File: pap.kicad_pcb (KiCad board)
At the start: 2 copper layers, 60 x 60 mm, 70 parts, among them J51 Conn_01x04, J52 Conn_01x02, J53 Conn_01x02, J54 RJ45, J55 RJ45, J56 RJ12, U1 powerstep01

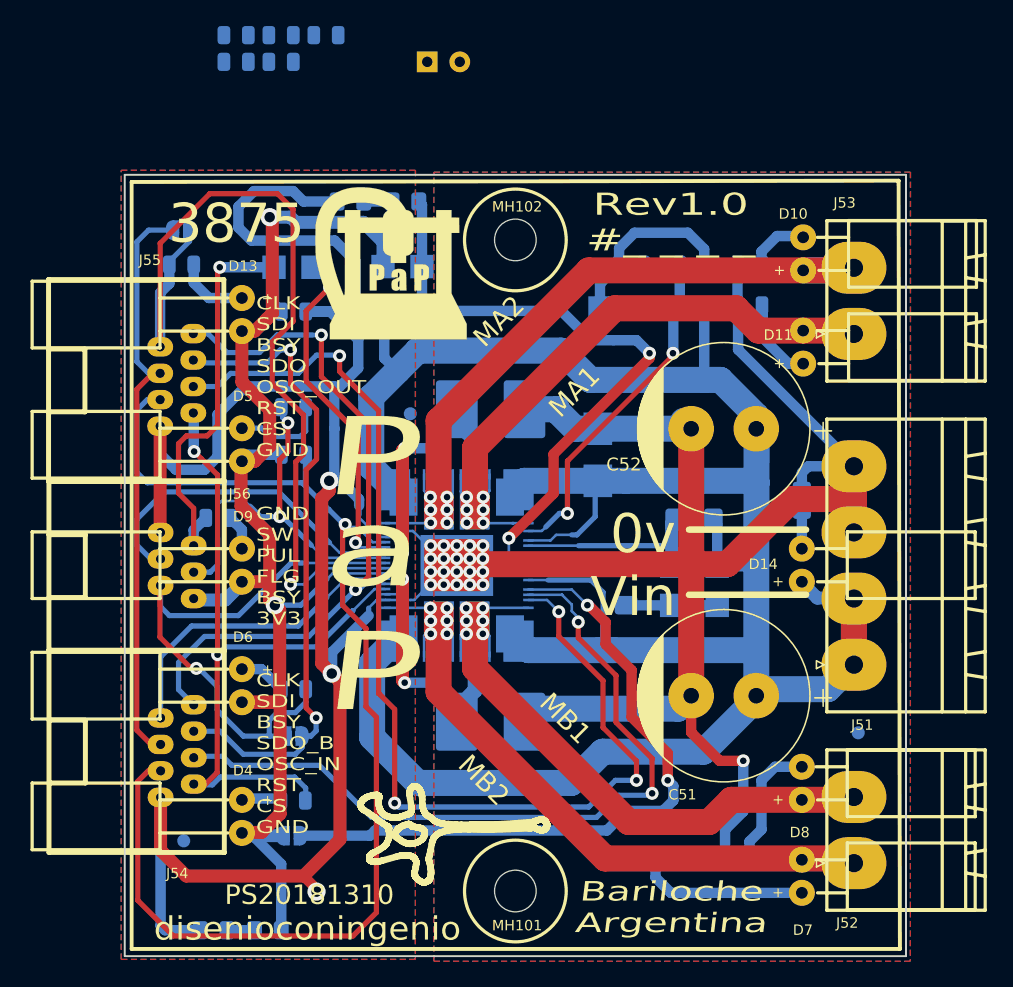
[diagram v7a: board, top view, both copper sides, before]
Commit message: termino ruteo, genero gerbers y drills, y entrego
Listo pisto, lo dejo asi, ya lo revise varias veces, agregue los
desacoples y el bulk pendiente, coloreo leds con nuevo 3d, genero
gerners, y agrego valores a los componentes. ha y tambien dejo PTH los
agujeros de los tornillos, quedan mejor. y no mucho mas.. entrego ya!
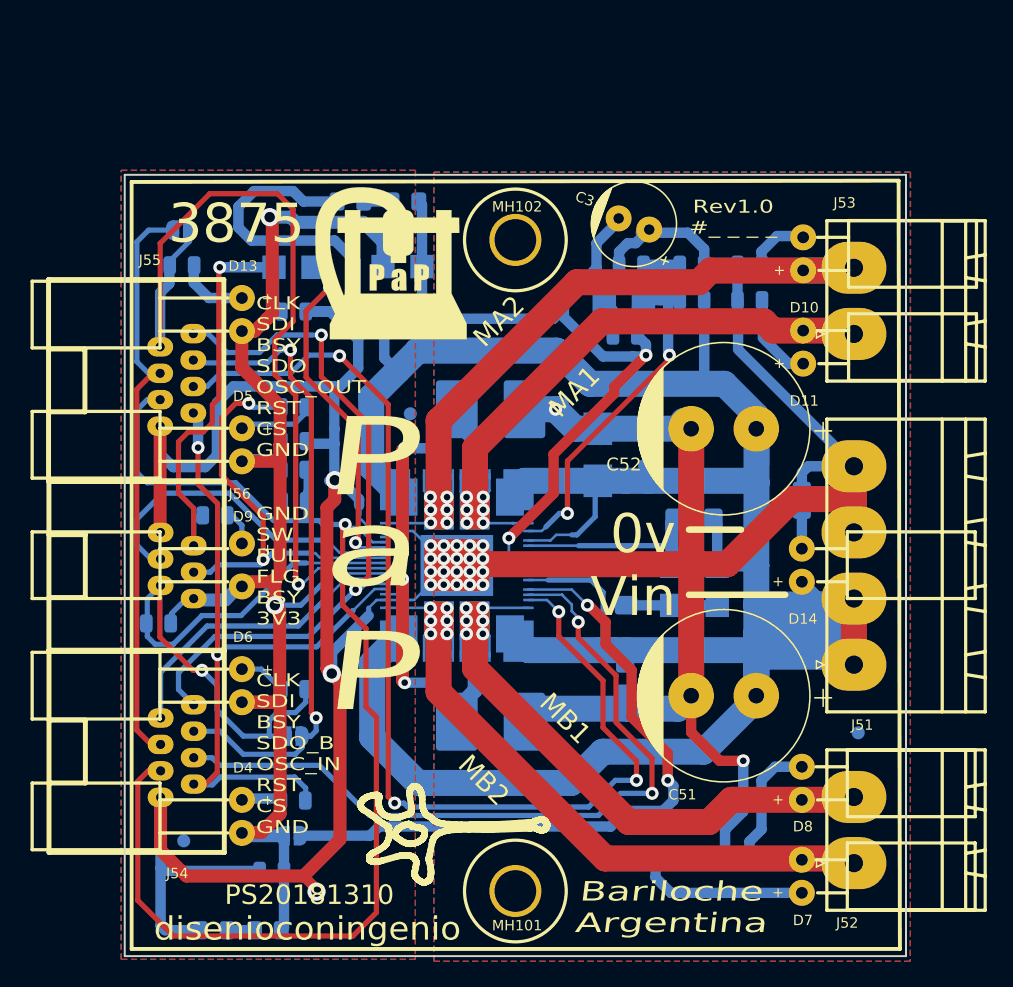
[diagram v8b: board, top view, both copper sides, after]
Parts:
- removed R204: R, pap:R_0805_2012Metric
- added C10: C, pap:C_0805_2012Metric, B.Cu at (130.9, 121.2)
- added C11: C, pap:C_0805_2012Metric, B.Cu at (132.6, 103.9)
- added R17: 100e, pap:R_0805_2012Metric, B.Cu at (96.9, 89.4)
- C1: value C -> 10n
- C3: footprint Capacitor_THT:CP_Radial_D6.3mm_P2.50mm -> pap:CP_Radial_D6.3mm_P2.50mm; moved to F.Cu
- C4, C5: value C -> 220n
- C6, C9: value C -> 100n
- D10, D7: footprint pap:led5p_enchufable -> pap:led5x2_enchufable_amarillo
- D11, D8: footprint pap:led5p_enchufable -> pap:led5x2_enchufable_verde
- D12: value D_Zener -> 3v3
- D13, D4: footprint pap:led5p_rj -> pap:led5x2_rj_verde
- D14: footprint pap:led5p_enchufable -> pap:led5x2_enchufable_rojo
- D5, D6: footprint pap:led5p_rj -> pap:led5x2_rj_amarillo
- D9: footprint pap:led5p_rj -> pap:led5x2_rj_rojo_abierto
- MH101, MH102: value MountingHole -> 3mm
- R1, R11, R12, R13, R14: value R -> 10k
- R10, R5, R8, R9: value R -> 100e
- R16: renamed from R203; value R -> 100e
- R18: renamed from R202; value R -> 10k
- R2: value R -> 1k5
- R3, R4: value R -> 0.1e
- R6: value R -> 100k
- R7: value R -> 3k3
- moved C2 64.3 mm to (103.8, 135.9)
- moved R15 43.5 mm to (95.1, 116.9)
- moved C9 36.0 mm to (105.5, 107.5), turned to 180 degrees
- moved C7 35.1 mm to (130.9, 94.8)
- moved C8 29.1 mm to (105.5, 102.9), turned to 180 degrees
- moved C3 21.4 mm to (132.8, 86.7), turned to 160 degrees
- moved R1 1.15 mm to (105.5, 105.1)
- moved D12 0.58 mm to (130.8, 92.2)
- moved R14 0.40 mm to (140.5, 92.1)
- moved R6 0.40 mm to (136.1, 92.1)
- moved R16 0.31 mm to (99.4, 108.6)
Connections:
- C3 pad 1: G3V3 -> G85V
- C3 pad 2: 3V3 -> 15v
- C8 pad 1: G85V -> G3V3
- C8 pad 2: 15v -> 3V3
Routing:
- net 85v: track 202.1 -> 222.1 mm
- net 15v: track 52.8 -> 63.2 mm
- net G3V3: track 153.2 -> 163.3 mm
- net 3V3: track 104.7 -> 113.4 mm
- net /connector/Busy: track 44.2 -> 48.9 mm
- net G85V: track 185.5 -> 190.1 mm, vias 21 -> 22
- net /connector/Flag: track 30.8 -> 33.4 mm
- net /connector/Reset: track 93.0 -> 94.6 mm
- net /connector/SDO: track 68.8 -> 67.4 mm
- net /connector/MotorA1: track 57.1 -> 56.3 mm
- net Net-(D9-Pad1): track 2.73 -> 3.53 mm
- net /connector/SDI: track 24.8 -> 24.1 mm
- net /connector/Busy_Out: track 50.9 -> 50.2 mm
- net Net-(D5-Pad1): track 7.18 -> 6.55 mm
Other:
- net class Default: clearance 0.2 -> 0.25
- net class Sense: clearance 0.2 -> 0.25
- rule trace_clearance: 0.2 -> 0.25
- board text added: "3v3"
- board text removed: "3v3 Sel"
